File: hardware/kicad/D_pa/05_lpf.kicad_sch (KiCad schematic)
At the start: 39 parts

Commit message: Replace the transmit filters: harmonic suppression was illegal
Simulation of the output filters shows second-harmonic suppression
between 3 and 30 dB, where 43 dB is necessary below 30 MHz and 60 dB
above. On the 80/60 m position the second harmonic of 3.5 MHz is
3.4 dB down: the filter barely touches it. The transmitter would have
been out of specification on every band, and the board gives no sign
of it. Output power, SWR and efficiency all read correctly while the
harmonic radiates.

The cause is the band grouping. One position must pass 5.37 MHz, so
its cutoff is at 6.0, and the second harmonic of the same position's
lowest band, 3.5 MHz, falls at 7.0. More poles do not help: by the
Chebyshev attenuation formula, nine poles give 32 dB there.

Each series inductor now has a parallel capacitor that places a
transmission zero on the harmonic. 80 m and 60 m are separate
positions, because a trap at 7.0 MHz also attenuates a 5.37 MHz
passband. That uses the seventh relay, which was a bypass; a
transmitter with no harmonic filter in line is not legal in any case.

  band      loss   2nd harmonic   was
  160m      0.61   -82.4          -25.2
  80m       0.64   -80.7          grouped
  60m       0.45   -81.9          grouped
  40_30m    1.45   -58.0          -9.5
  20_17m    0.88   -68.4          -18.2
  15_10m    1.35   -61.0          -14.1
  6m        1.14   -82.8          -30.2
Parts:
- removed C504: 1600pF, Capacitor_THT:C_Disc_D7.5mm_W5.0mm_P5.00mm, symbol Device:C
- removed C515, C522: 200pF, Capacitor_THT:C_Disc_D7.5mm_W5.0mm_P5.00mm, symbol Device:C
- removed C525, C529: 68pF, Capacitor_THT:C_Disc_D7.5mm_W5.0mm_P5.00mm, symbol Device:C
- removed L503: T94-2 25s, dogrudan-sdr:L_Toroid_T94_Vertical, symbol Device:L
- removed L506: T94-2 15s, dogrudan-sdr:L_Toroid_T94_Vertical, symbol Device:L
- removed L513: T68-2 13s, dogrudan-sdr:L_Toroid_T68_Vertical, symbol Device:L
- removed L516: T68-2 10s, dogrudan-sdr:L_Toroid_T68_Vertical, symbol Device:L
- removed L521, L523: T50-6 10s, dogrudan-sdr:L_Toroid_T50_Vertical, symbol Device:L
- removed L526, L528: T50-6 8s, dogrudan-sdr:L_Toroid_T50_Vertical, symbol Device:L
- added C503: 2700pF, Capacitor_THT:C_Disc_D7.5mm_W5.0mm_P5.00mm, symbol Device:C
- added C506: 1600pF, Capacitor_THT:C_Disc_D7.5mm_W5.0mm_P5.00mm, symbol Device:C
- added C513: 820pF, Capacitor_THT:C_Disc_D7.5mm_W5.0mm_P5.00mm, symbol Device:C
- added C516: 120pF, Capacitor_THT:C_Disc_D7.5mm_W5.0mm_P5.00mm, symbol Device:C
- added C521, C531: 270pF, Capacitor_THT:C_Disc_D7.5mm_W5.0mm_P5.00mm, symbol Device:C
- added C523: 180pF, Capacitor_THT:C_Disc_D7.5mm_W5.0mm_P5.00mm, symbol Device:C
- added C526: 75pF, Capacitor_THT:C_Disc_D7.5mm_W5.0mm_P5.00mm, symbol Device:C
- added C528, C534, C538: 160pF, Capacitor_THT:C_Disc_D7.5mm_W5.0mm_P5.00mm, symbol Device:C
- added C530: 68pF, Capacitor_THT:C_Disc_D7.5mm_W5.0mm_P5.00mm, symbol Device:C
- added C533: 30pF, Capacitor_THT:C_Disc_D7.5mm_W5.0mm_P5.00mm, symbol Device:C
- added C535, C541: 91pF, Capacitor_THT:C_Disc_D7.5mm_W5.0mm_P5.00mm, symbol Device:C
- added C537: 51pF, Capacitor_THT:C_Disc_D7.5mm_W5.0mm_P5.00mm, symbol Device:C
- added C540: 24pF, Capacitor_THT:C_Disc_D7.5mm_W5.0mm_P5.00mm, symbol Device:C
- added C542, C548: 62pF, Capacitor_THT:C_Disc_D7.5mm_W5.0mm_P5.00mm, symbol Device:C
- added C544: 15pF, Capacitor_THT:C_Disc_D7.5mm_W5.0mm_P5.00mm, symbol Device:C
- added C545: 110pF, Capacitor_THT:C_Disc_D7.5mm_W5.0mm_P5.00mm, symbol Device:C
- added C547: 6.2pF, Capacitor_THT:C_Disc_D7.5mm_W5.0mm_P5.00mm, symbol Device:C
- added L504: T94-2 24s, dogrudan-sdr:L_Toroid_T94_Vertical, symbol Device:L
- added L515: T94-2 15s, dogrudan-sdr:L_Toroid_T94_Vertical, symbol Device:L
- added L522, L525: T68-2 12s, dogrudan-sdr:L_Toroid_T68_Vertical, symbol Device:L
- added L529, L532: T68-2 10s, dogrudan-sdr:L_Toroid_T68_Vertical, symbol Device:L
- added L536, L539: T50-6 9s, dogrudan-sdr:L_Toroid_T50_Vertical, symbol Device:L
- added L543, L546: T50-6 7s, dogrudan-sdr:L_Toroid_T50_Vertical, symbol Device:L
- C502: value 3000pF -> 430pF
- C505: value 620pF -> 180pF
- C507: value 1000pF -> 820pF
- C509: value 620pF -> 220pF
- C510: value 330pF -> 1500pF
- C512: value 560pF -> 91pF
- C514: value 330pF -> 560pF
- C517: value 330pF -> 1000pF
- C519: value 200pF -> 56pF
- C520: value 120pF -> 560pF
- C524: value 120pF -> 430pF
- C527: value 110pF -> 270pF
- L501: value T94-2 25s -> T94-2 24s
- L508: value T94-2 15s -> T94-2 17s
- L511: value T68-2 13s -> T94-2 17s; footprint dogrudan-sdr:L_Toroid_T68_Vertical -> dogrudan-sdr:L_Toroid_T94_Vertical
- L518: value T68-2 10s -> T94-2 15s; footprint dogrudan-sdr:L_Toroid_T68_Vertical -> dogrudan-sdr:L_Toroid_T94_Vertical
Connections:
- net GND: now also C503.2, C506.2, C513.2, C521.2, C528.2, C531.2, C534.2, C535.2, C538.2, C541.2, C542.2, C545.2, C548.2; no longer C502.2, C505.2, C509.2, C512.2, C519.2
- net LF1_A: now also C502.1
- net LF1_B: now also C505.2, C506.1, L504.2
- net LF2_A: now also C507.1, C509.1, L508.1; no longer C505.1
- net LF2_B: now also C512.2, L511.2, C513.1; no longer C509.1, L508.2
- net LF3_A: now also C514.1, C516.1, L515.1; no longer C510.1, L511.1
- net LF3_B: now also C519.2, C520.1, L518.2; no longer C514.1
- net LF4_A: now also C521.1, C523.1, L522.1
- net LF4_B: now also C527.1, C526.2, L525.2; no longer C519.1, L518.2
- net LF5_A: now also C528.1, C530.1, L529.1; no longer C520.1
- net LF5_B: now also C533.2, C534.1, L532.2; no longer C524.1
- net LF6_A: now also C535.1, C537.1, L536.1
- net LF6_B: now also C540.2, C541.1, L539.2
- net N1_1: now also C502.2, C505.1, C503.1, L504.1; no longer C502.1
- net N2_1: now also C509.2, C510.1, C512.1, L508.2, L511.1; no longer C507.1, L508.1
- net N3_1: now also C517.1, C519.1, L518.1, C516.2, L515.2; no longer C512.1, L511.2
- net N4_1: now also C524.1, C523.2, C526.1, L522.2, L525.1; no longer C517.1, L518.1
- net N5_1: now also C530.2, C531.1, C533.1, L529.2, L532.1
- net N6_1: now also C537.2, C538.1, C540.1, L536.2, L539.1; no longer C527.1
- net PA_LPF_OUT: no longer KL7.14 (NO1), KL7.24 (NO2)
- new net LF7_A: C542.1, C544.1, KL7.14 (NO1), L543.1
- new net LF7_B: C547.2, C548.1, KL7.24 (NO2), L546.2
- new net N7_1: C544.2, C545.1, C547.1, L543.2, L546.1

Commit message: Name the copyright holder and stamp it into the generated files
The repository had three licence files and no statement of who owns
the work. The only record of authorship was the git author field.

Copyleft depends on that statement. GPL and CERN-OHL-S work because
the holder grants permission on condition of reciprocity; with no
holder named there is nobody to require it from a downstream user.
Naming the author keeps the design open rather than closing it.

kicad/telif.py is the single source. The line reaches the schematics
through their title block and not through the generators, because
every schematic file is rewritten on each build and a header placed in
a generator would disappear at the first regeneration. All 23
schematics carry it. 109 source files have SPDX headers, split by the
project's own table: generators and the layout chain are hardware
under CERN-OHL-S-2.0, HDL and the audit tools are software under
GPL-3.0-only.

Board C's inductors also move to footprints that match parts that can
be bought. All of them sat on 0805 pads. Of the values this design
needs, 33 to 220 nH are 0603 parts, 470 and 820 nH are 0805, and
everything from 1000 nH upward is 1210, which is 3.2 by 2.5 mm and
does not fit an 0805 land. 32 inductors could not have been soldered.

A symbol-against-footprint check cannot find this. Those two agreed
with each other; what was wrong was the body size of the real part
behind the footprint.
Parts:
- removed C505, C523: 180pF, Capacitor_THT:C_Disc_D7.5mm_W5.0mm_P5.00mm, symbol Device:C
- removed C510: 1500pF, Capacitor_THT:C_Disc_D7.5mm_W5.0mm_P5.00mm, symbol Device:C
- removed C514: 560pF, Capacitor_THT:C_Disc_D7.5mm_W5.0mm_P5.00mm, symbol Device:C
- removed C519: 56pF, Capacitor_THT:C_Disc_D7.5mm_W5.0mm_P5.00mm, symbol Device:C
- removed C528: 160pF, Capacitor_THT:C_Disc_D7.5mm_W5.0mm_P5.00mm, symbol Device:C
- removed C537: 51pF, Capacitor_THT:C_Disc_D7.5mm_W5.0mm_P5.00mm, symbol Device:C
- removed C541: 91pF, Capacitor_THT:C_Disc_D7.5mm_W5.0mm_P5.00mm, symbol Device:C
- removed L504: T94-2 24s, dogrudan-sdr:L_Toroid_T94_Vertical, symbol Device:L
- removed L508, L511: T94-2 17s, dogrudan-sdr:L_Toroid_T94_Vertical, symbol Device:L
- removed L515, L518: T94-2 15s, dogrudan-sdr:L_Toroid_T94_Vertical, symbol Device:L
- removed L522, L525: T68-2 12s, dogrudan-sdr:L_Toroid_T68_Vertical, symbol Device:L
- removed L529: T68-2 10s, dogrudan-sdr:L_Toroid_T68_Vertical, symbol Device:L
- removed L536, L539: T50-6 9s, dogrudan-sdr:L_Toroid_T50_Vertical, symbol Device:L
- removed L543: T50-6 7s, dogrudan-sdr:L_Toroid_T50_Vertical, symbol Device:L
- added C504: 2700pF, Capacitor_THT:C_Disc_D7.5mm_W5.0mm_P5.00mm, symbol Device:C
- added C508: 1600pF, Capacitor_THT:C_Disc_D7.5mm_W5.0mm_P5.00mm, symbol Device:C
- added C511: 200pF, Capacitor_THT:C_Disc_D7.5mm_W5.0mm_P5.00mm, symbol Device:C
- added C515, C553: 91pF, Capacitor_THT:C_Disc_D7.5mm_W5.0mm_P5.00mm, symbol Device:C
- added C518: 560pF, Capacitor_THT:C_Disc_D7.5mm_W5.0mm_P5.00mm, symbol Device:C
- added C522: 1000pF, Capacitor_THT:C_Disc_D7.5mm_W5.0mm_P5.00mm, symbol Device:C
- added C525, C543: 3.6pF, Capacitor_SMD:C_1206_3216Metric, symbol Device:C
- added C529, C536, C549: 160pF, Capacitor_THT:C_Disc_D7.5mm_W5.0mm_P5.00mm, symbol Device:C
- added C539: 6.8pF, Capacitor_SMD:C_1206_3216Metric, symbol Device:C
- added C551: 22pF, Capacitor_THT:C_Disc_D7.5mm_W5.0mm_P5.00mm, symbol Device:C
- added C552: 1.6pF, Capacitor_SMD:C_1206_3216Metric, symbol Device:C
- added C554, C562: 62pF, Capacitor_THT:C_Disc_D7.5mm_W5.0mm_P5.00mm, symbol Device:C
- added C556: 13pF, Capacitor_THT:C_Disc_D7.5mm_W5.0mm_P5.00mm, symbol Device:C
- added C557: 1.1pF, Capacitor_SMD:C_1206_3216Metric, symbol Device:C
- added C558: 110pF, Capacitor_THT:C_Disc_D7.5mm_W5.0mm_P5.00mm, symbol Device:C
- added C560: 5.1pF, Capacitor_THT:C_Disc_D7.5mm_W5.0mm_P5.00mm, symbol Device:C
- added C561: 1.2pF, Capacitor_SMD:C_1206_3216Metric, symbol Device:C
- added L505: T94-2 24s, dogrudan-sdr:L_Toroid_T94_Vertical, symbol Device:L
- added L510, L514: T94-2 17s, dogrudan-sdr:L_Toroid_T94_Vertical, symbol Device:L
- added L519, L523: T94-2 15s, dogrudan-sdr:L_Toroid_T94_Vertical, symbol Device:L
- added L528: T68-2 12s, dogrudan-sdr:L_Toroid_T68_Vertical, symbol Device:L
- added L537, L541: T68-2 10s, dogrudan-sdr:L_Toroid_T68_Vertical, symbol Device:L
- added L550: T50-6 9s, dogrudan-sdr:L_Toroid_T50_Vertical, symbol Device:L
- added L555, L559: T50-6 7s, dogrudan-sdr:L_Toroid_T50_Vertical, symbol Device:L
- C502: value 430pF -> 360pF
- C503: value 2700pF -> 56pF; footprint Capacitor_THT:C_Disc_D7.5mm_W5.0mm_P5.00mm -> Capacitor_SMD:C_1206_3216Metric
- C506: value 1600pF -> 180pF
- C507: value 820pF -> 4.7pF; footprint Capacitor_THT:C_Disc_D7.5mm_W5.0mm_P5.00mm -> Capacitor_SMD:C_1206_3216Metric
- C509: value 220pF -> 820pF
- C512: value 91pF -> 15pF; footprint Capacitor_THT:C_Disc_D7.5mm_W5.0mm_P5.00mm -> Capacitor_SMD:C_1206_3216Metric
- C513: value 820pF -> 1500pF
- C516: value 120pF -> 4.7pF; footprint Capacitor_THT:C_Disc_D7.5mm_W5.0mm_P5.00mm -> Capacitor_SMD:C_1206_3216Metric
- C517: value 1000pF -> 820pF
- C520: value 560pF -> 120pF
- C521: value 270pF -> 3pF; footprint Capacitor_THT:C_Disc_D7.5mm_W5.0mm_P5.00mm -> Capacitor_SMD:C_1206_3216Metric
- C524: value 430pF -> 51pF
- C526: value 75pF -> 560pF
- C530: value 68pF -> 12pF; footprint Capacitor_THT:C_Disc_D7.5mm_W5.0mm_P5.00mm -> Capacitor_SMD:C_1206_3216Metric
- C531: value 270pF -> 430pF
- C533: value 30pF -> 75pF
- C534: value 160pF -> 1.6pF; footprint Capacitor_THT:C_Disc_D7.5mm_W5.0mm_P5.00mm -> Capacitor_SMD:C_1206_3216Metric
- C535: value 91pF -> 270pF
- C538: value 160pF -> 62pF
- C540: value 24pF -> 270pF
- C542: value 62pF -> 27pF
- C544: value 15pF -> 160pF
- C545: value 110pF -> 91pF
- C547: value 6.2pF -> 51pF
- C548: value 62pF -> 2.2pF; footprint Capacitor_THT:C_Disc_D7.5mm_W5.0mm_P5.00mm -> Capacitor_SMD:C_1206_3216Metric
- L532: value T68-2 10s -> T68-2 12s
- L546: value T50-6 7s -> T50-6 9s
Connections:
- net GND: now also C509.2, C526.2, C540.2, C544.2, C504.2, C508.2, C518.2, C522.2, C536.2, C549.2, C553.2, C554.2, C558.2, C562.2; no longer C503.2, C506.2, C507.2, C520.2, C521.2, C524.2, C534.2, C538.2, C542.2, C548.2
- net LF1_A: now also C503.1
- net LF1_B: now also C506.2, C507.2, C508.1, L505.2; no longer C506.1
- net LF2_A: now also C512.1, C511.1, L510.1; no longer C507.1
- net LF2_B: now also C516.2, C517.1, C515.2, L514.2; no longer C512.2, C513.1
- net LF3_A: now also C520.1, C521.1, C518.1, L519.1; no longer C516.1
- net LF3_B: now also C524.2, C526.1, C525.2, L523.2; no longer C520.1
- net LF4_A: now also C527.1, C530.1, C529.1, L528.1; no longer C521.1
- net LF4_B: now also C533.2, C534.2, C535.1, L532.2; no longer C526.2, C527.1
- net LF5_A: now also C538.1, C536.1, C539.1, L537.1; no longer C530.1
- net LF5_B: now also C542.2, C544.1, C543.2, L541.2; no longer C533.2, C534.1, L532.2
- net LF6_A: now also C545.1, C547.1, C548.1, L546.1; no longer C535.1
- net LF6_B: now also C551.2, C552.2, C553.1, L550.2; no longer C540.2
- net LF7_A: now also C554.1, C556.1, C557.1, L555.1; no longer C542.1, C544.1
- net LF7_B: now also C560.2, C561.2, C562.1, L559.2; no longer C547.2, C548.1, L546.2
- net N1_1: now also C503.2, C506.1, C507.1, C504.1, L505.1; no longer C503.1
- net N2_1: now also C512.2, C513.1, C516.1, C511.2, C515.1, L510.2, L514.1; no longer C509.2, C512.1
- net N3_1: now also C520.2, C521.2, C524.1, C522.1, C525.1, L519.2, L523.1; no longer C516.2, C517.1
- net N4_1: now also C530.2, C531.1, C533.1, C534.1, L532.1, C529.2, L528.2; no longer C524.1, C526.1
- net N5_1: now also C538.2, C540.1, C542.1, C539.2, C543.1, L537.2, L541.1; no longer C530.2, C531.1, C533.1, L532.1
- net N6_1: now also C547.2, C548.2, L546.2, C549.1, C551.1, C552.1, L550.1; no longer C538.1, C540.1
- net N7_1: now also C556.2, C557.2, C558.1, C560.1, C561.1, L555.2, L559.1; no longer C544.2, C545.1, C547.1, L546.1

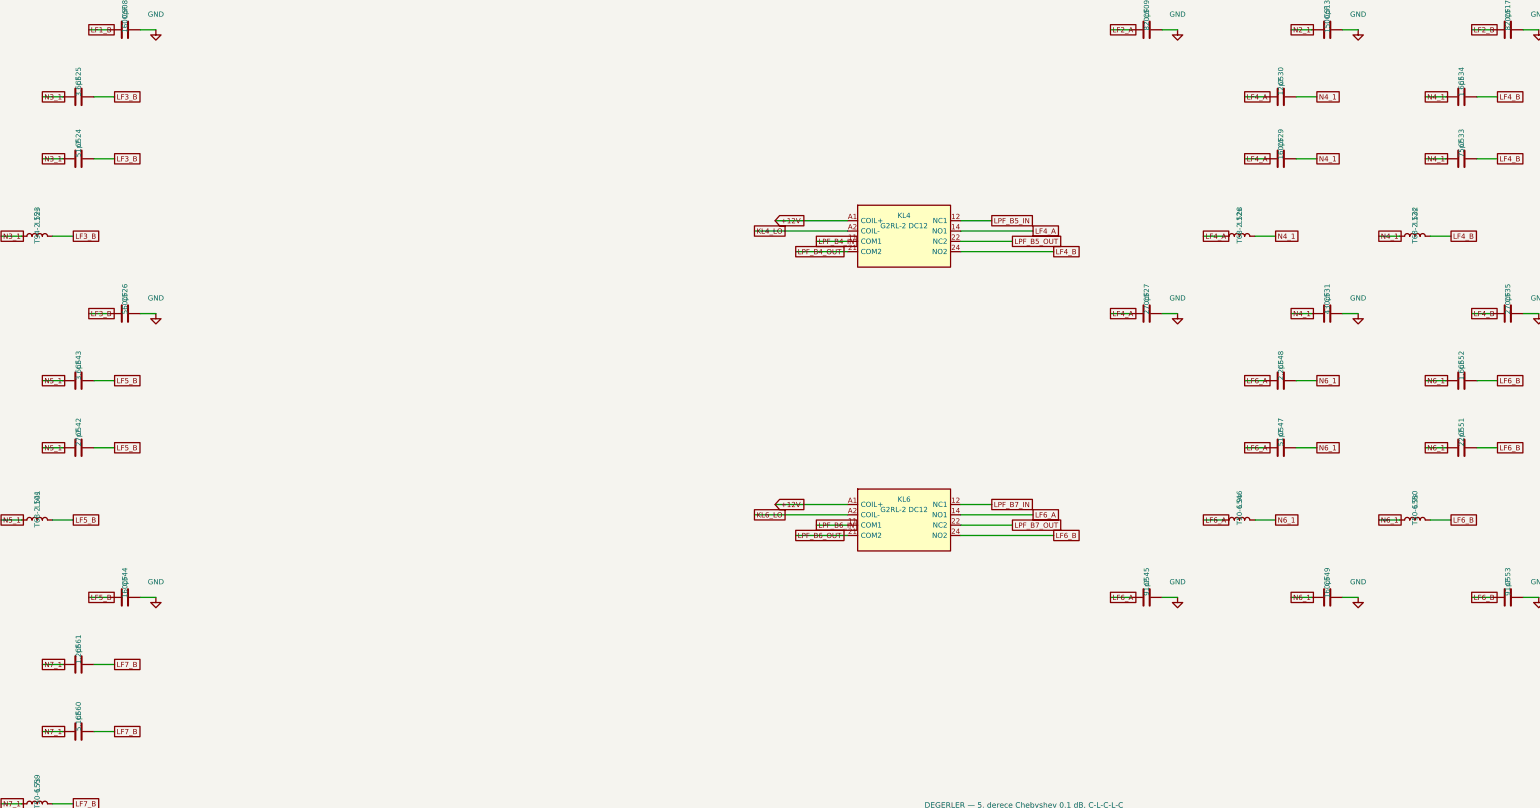
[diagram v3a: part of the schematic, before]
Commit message: Correct the voltage rating of the RF capacitors on board D
The BOM had no verified order code for 245 parts. The BOM program
recognised the format of a value and wrote "BASE" for all of them. It
did not examine availability.

A new tool queries the supplier. It does not accept "the part
exists". The package and the value must agree exactly. The stock must
be more than the quantity. It also reads the properties of the part.

Two faults came out of this:

The trap capacitors were 50 V parts. The carrier peak voltage is
100 V at 100 W into 50 ohms, and the voltage across the trap inductor
is 93 V. A 50 V part shows the same value in the catalogue and then
breaks down. The fault appears only when the transmitter operates.

The 1.1 pF, 1.6 pF and 3.6 pF values had no stock in the 1206
package. The same values are available in 0603 at 250 V. The smaller
package is acceptable here. This capacitor is the small half of a
pair and carries a small part of the current.

The value selection now depends on availability. The program found
the nearest pair mathematically, and one value was 3.6 pF. That value
has no stock at 250 V in any package. The small half now comes from a
list of parts that are really in stock.

The harmonic suppression did not change: 58.7 dB to 83.8 dB, against
a limit of 43 dB and 60 dB.

The filter capacitors were X7R parts. The capacitance of X7R changes
with voltage and with temperature. Every capacitor below 10 nF is now
a filter part and must be C0G or NP0.

Through-hole parts do not go into machine assembly. A separate file
lists them with the necessary specification. The BOM gave only the
value and a general footprint, and that invites the wrong purchase.
At 100 W, 1.3 A flows through the shunt capacitor at 14 MHz. A cheap
disc ceramic heats, its capacitance moves, and the filter changes.
Only full transmitter power shows this.
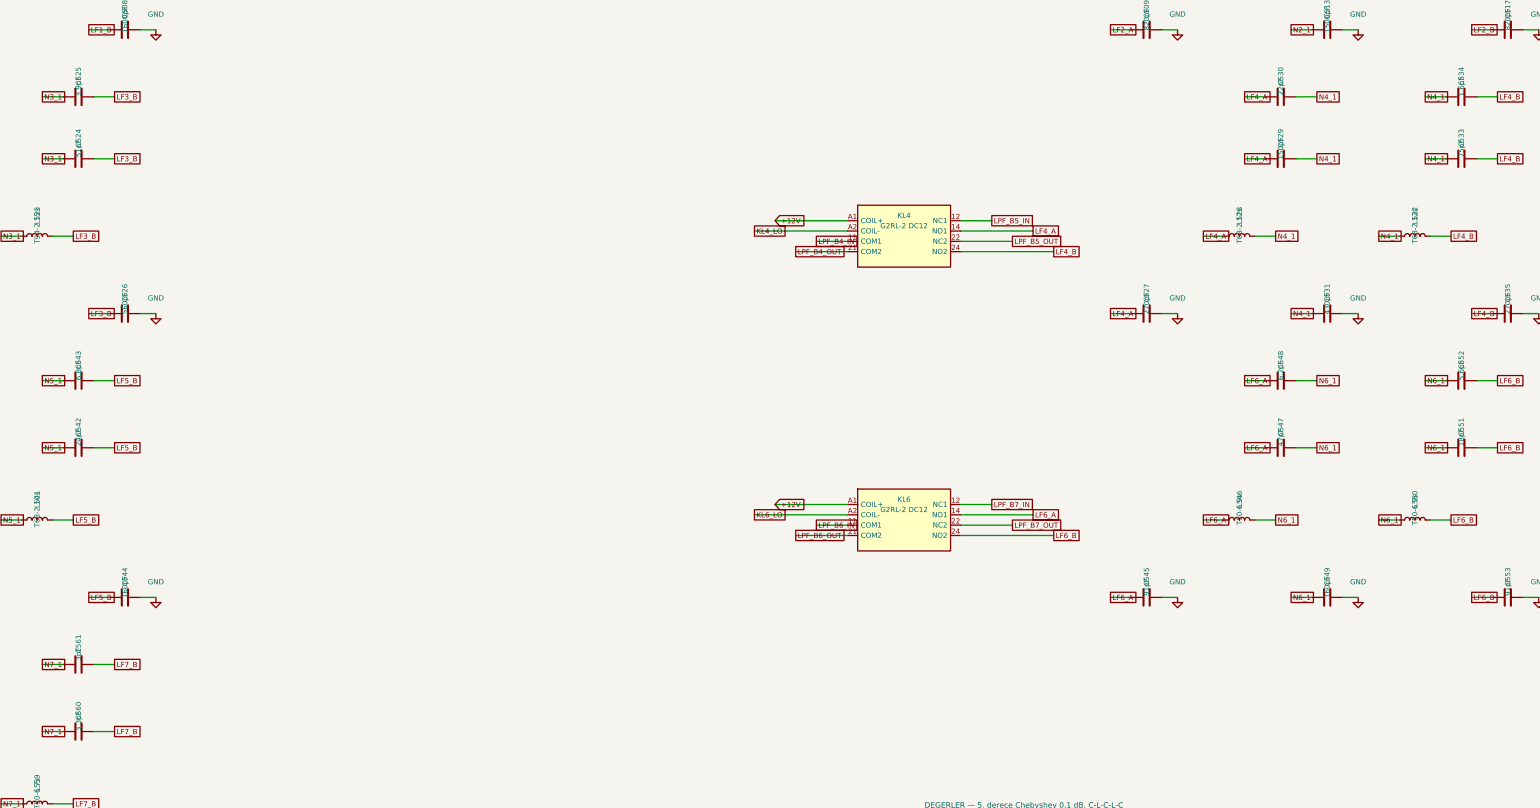
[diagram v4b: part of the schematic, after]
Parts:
- C503, C507, C512, C516, C521, C534, C539, C557: footprint Capacitor_SMD:C_1206_3216Metric -> Capacitor_SMD:C_0603_1608Metric
- C525: value 3.6pF -> 3.9pF; footprint Capacitor_SMD:C_1206_3216Metric -> Capacitor_SMD:C_0603_1608Metric
- C529: value 160pF -> 150pF
- C530: value 12pF -> 22pF; footprint Capacitor_SMD:C_1206_3216Metric -> Capacitor_SMD:C_0603_1608Metric
- C542: value 27pF -> 24pF
- C543: value 3.6pF -> 6.8pF; footprint Capacitor_SMD:C_1206_3216Metric -> Capacitor_SMD:C_0603_1608Metric
- C547: value 51pF -> 47pF
- C548: value 2.2pF -> 6.2pF; footprint Capacitor_SMD:C_1206_3216Metric -> Capacitor_SMD:C_0603_1608Metric
- C551: value 22pF -> 18pF
- C552: value 1.6pF -> 5.6pF; footprint Capacitor_SMD:C_1206_3216Metric -> Capacitor_SMD:C_0603_1608Metric
- C560: value 5.1pF -> 3.3pF
- C561: value 1.2pF -> 3pF; footprint Capacitor_SMD:C_1206_3216Metric -> Capacitor_SMD:C_0603_1608Metric
